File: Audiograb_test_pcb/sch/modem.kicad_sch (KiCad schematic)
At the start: 58 parts, among them J1 TestPoint, J18 3V7_in, J2 TestPoint, J3 TestPoint, J4 EMPCB.SMAFSTJ.B.HT, J4 TestPoint, J5 EMPCB.SMAFSTJ.B.HT, J5 TestPoint, J6 TestPoint, J7 TestPoint, J8 TestPoint, J9 TestPoint, P1 SF72S006VBDR2500, T1 SSM3J358R_LF, T1 T1, T10 TestPoint, T11 TestPoint, T2 T1, T3 T1, T4 T1, T5 T1, T6 T1, T7 TestPoint, T8 TestPoint, T9 TestPoint, U1 RC7620_1105027, U13 NX3008NBKW_115, U2 NX3008NBKW_115, U3 NX3008NBKW_115, U4 NX3008NBKW_115, U5 NX3008NBKW_115, U6 NX3008NBKW_115, U7 NX3008NBKW_115

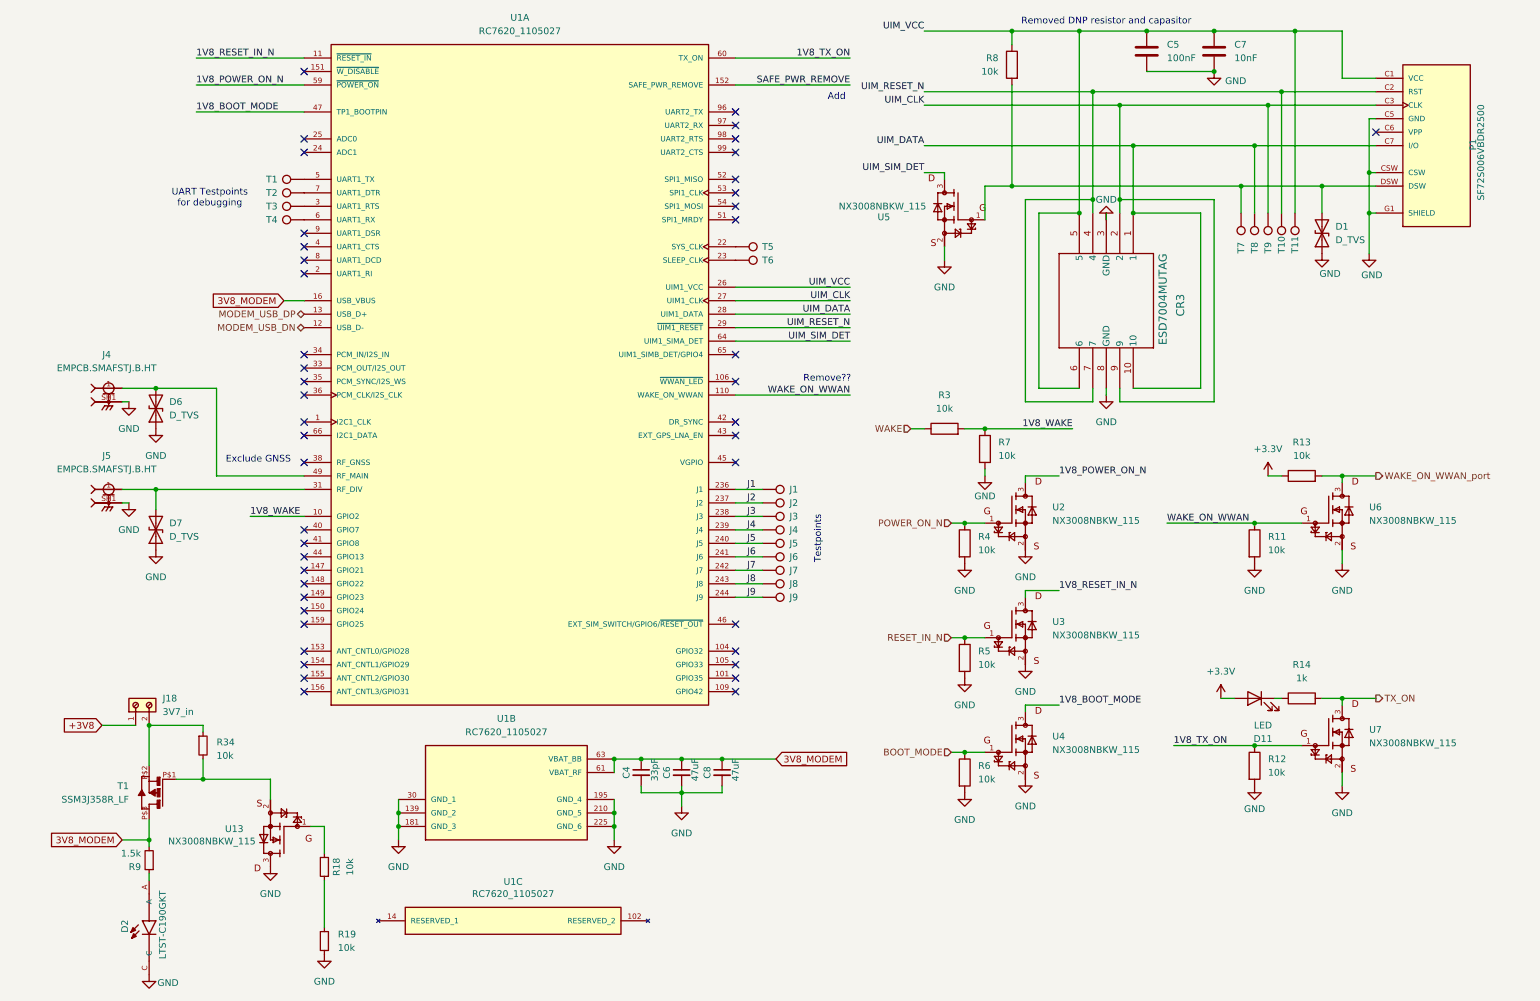
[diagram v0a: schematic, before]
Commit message: La til hard shutdown for modem, la til signal SAFE_PWR_REMOVE, fikset nummerering testpoints ++ noen småting
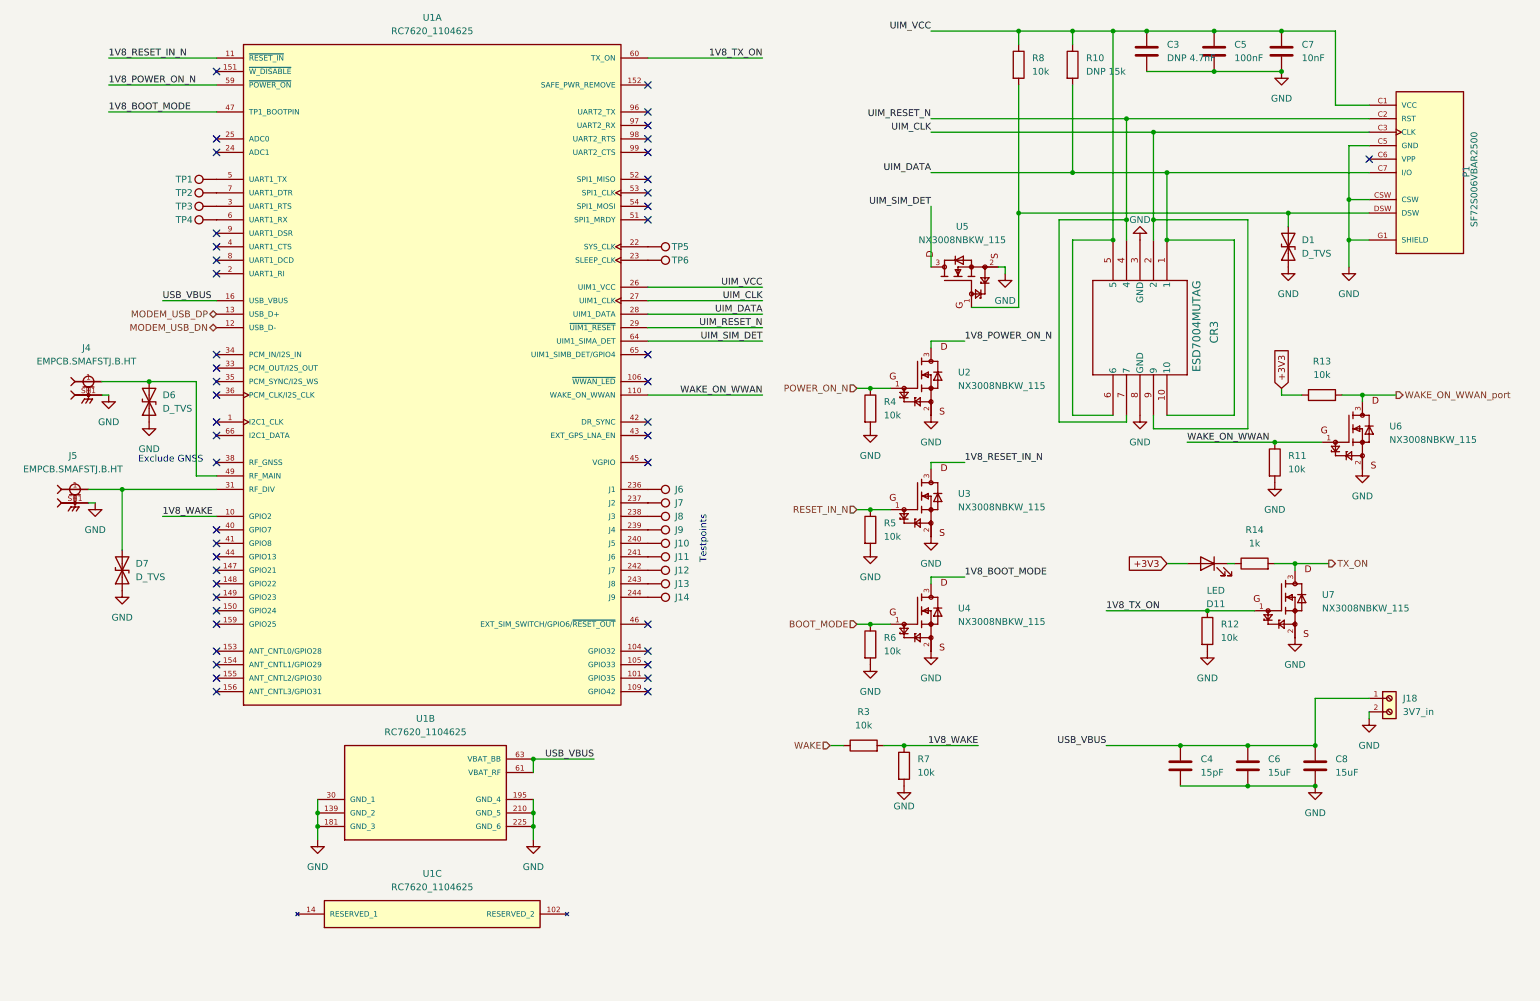
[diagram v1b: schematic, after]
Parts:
- removed C4: 33pF, Capacitor_SMD:C_0603_1608Metric, symbol Device:C_Small
- removed C6, C8: 47uF, Capacitor_SMD:C_1206_3216Metric, symbol Device:C_Small
- removed D2: LTST-C190GKT, LTST-C190GKT:LEDM1608X80, symbol LTST-C190GKT:LTST-C190GKT
- removed R18, R19, R34: 10k, Resistor_SMD:R_0603_1608Metric, symbol Device:R_Small
- removed R9: 1.5k, Resistor_SMD:R_0603_1608Metric, symbol Device:R_Small
- removed T1: SSM3J358R_LF, SSM3J358R_LF:TRANS_SSM3K333R_LF, symbol SSM3J338R_LF:SSM3J338R_LF
- removed T10, T11, T7, T8, T9: TestPoint, TestPoint:TestPoint_Loop_D2.60mm_Drill1.6mm_Beaded, symbol Connector:TestPoint
- removed U13: NX3008NBKW_115, NX3008NBKW_115:SOT65P210X110-3N, symbol NX3008NBKW_115:NX3008NBKW_115
- added C3: DNP 4.7nF, Capacitor_SMD:C_0603_1608Metric, symbol Device:C
- added C4: 15pF, Capacitor_SMD:C_0603_1608Metric, symbol Device:C
- added C6, C8: 15uF, Capacitor_SMD:C_0603_1608Metric, symbol Device:C
- added R10: DNP 15k, Resistor_SMD:R_0603_1608Metric, symbol Device:R
- CR3: footprint ESD7004MUTAG:UDFN10_517BB_ONS -> UDFN10_517BB_ONS
- P1: value SF72S006VBDR2500 -> SF72S006VBAR2500
- U1: value RC7620_1105027 -> RC7620_1104625
- renumbered J5 to J10, J6 to J11, J7 to J12, J8 to J13, J9 to J14, J1 to J6, J2 to J7, J3 to J8, J4 to J9, T1 to TP1, T2 to TP2, T3 to TP3, T4 to TP4, T5 to TP5, T6 to TP6
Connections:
- net +3V8 is gone; now on net VBAT_BB: J18.1
- net GND: now also J18.2, C3.2, C4.2, C6.2, C8.2
- net UIM_DATA: now also R10.2
- net UIM_VCC: now also C3.1, R10.1
- net VBAT_BB: now also C4.1, C6.1, C8.1
- net +3.3V renamed +3V3
- net J1: no longer names the net of J6.1, U1.236 (J1)
- net J2: no longer names the net of J7.1, U1.237 (J2)
- net J3: no longer names the net of J8.1, U1.238 (J3)
- net J4: no longer names the net of J9.1, U1.239 (J4)
- net J5: no longer names the net of J10.1, U1.240 (J5)
- net J6: no longer names the net of J11.1, U1.241 (J6)
- net J7: no longer names the net of J12.1, U1.242 (J7)
- net J8: no longer names the net of J13.1, U1.243 (J8)
- net J9: no longer names the net of J14.1, U1.244 (J9)
- net SAFE_PWR_REMOVE: no longer names the net of U1.152 (SAFE_PWR_REMOVE)
- no-connect marks 45 -> 46
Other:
- note removed: "Add"
- note removed: "Remove??"
- note removed: "Removed DNP resistor and capasitor"
- note removed: "UART Testpoints for debugging"
- moved on the sheet: C5, C7, CR3, D1, D11, D6, D7, J10, J11, J12, J13, J14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
